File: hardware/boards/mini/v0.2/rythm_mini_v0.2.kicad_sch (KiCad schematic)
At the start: 99 parts, among them IC1 NAU88C22YG, IC3 IS42S16160J-6BLI, J2 Top, J3 Bottom, Q1 PMV37EN22, U1 W25Q128JVP, U2 LTV-217-G, U4 STM32H750XBHx, Y1 Crystal_GND24, Y3 Crystal

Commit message: mini: start BOM selection
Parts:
- C10, C11, C12, C13, C14, C33, C48, C5, C50, C51, C52, C54, C55, C56, C57, C58, C60, C61, C62, C63, C64, C67, C68, C7, C8, C9: JLC (none) -> C1525
- C16, C17, C18, C19, C28, C29, C36, C37, C38: JLC (none) -> C23733
- C20, C21, C22, C23, C24, C25, C26, C27, C31, C32, C6: JLC (none) -> C52923
- C30: JLC (none) -> C15195
- C34, C35, C69: JLC (none) -> C15525
- D1: footprint LED_SMD:LED_0402_1005Metric -> LED_SMD:LED_0603_1608Metric; JLC (none) -> C2286
- D2, D4: footprint LED_SMD:LED_0402_1005Metric -> LED_SMD:LED_0603_1608Metric; JLC (none) -> C89811
- IC3: JLC (none) -> C1351289
- J2, J3: JLC (none) -> C424647
- Q1: JLC (none) -> C478164
- R1, R2: JLC (none) -> C25900
- R10, R11, R12, R13, R14, R18, R5: JLC (none) -> C25744
- R3, R4: JLC (none) -> C25879
- R7: JLC (none) -> C25091
- U4: JLC (none) -> C405932
- Y3: value Crystal -> 32.768kHz

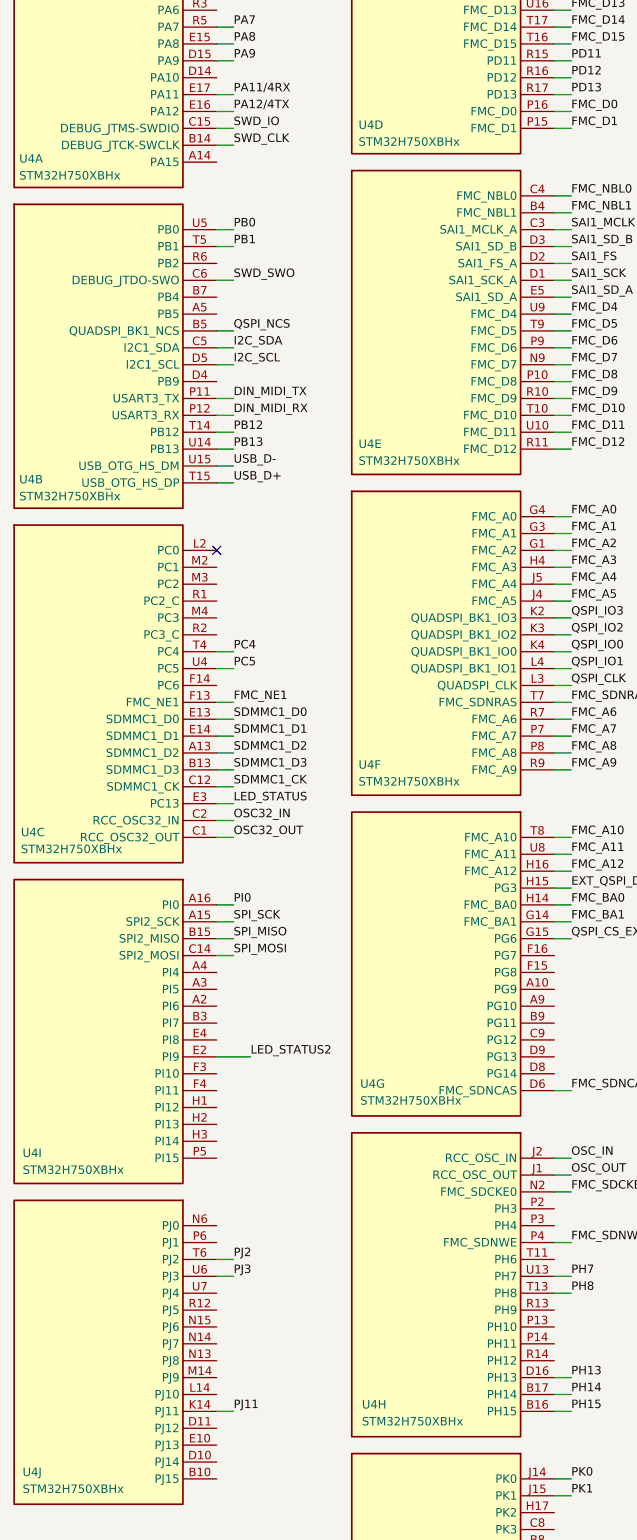
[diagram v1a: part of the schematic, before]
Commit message: mini: add Digikey part numbers to BOM
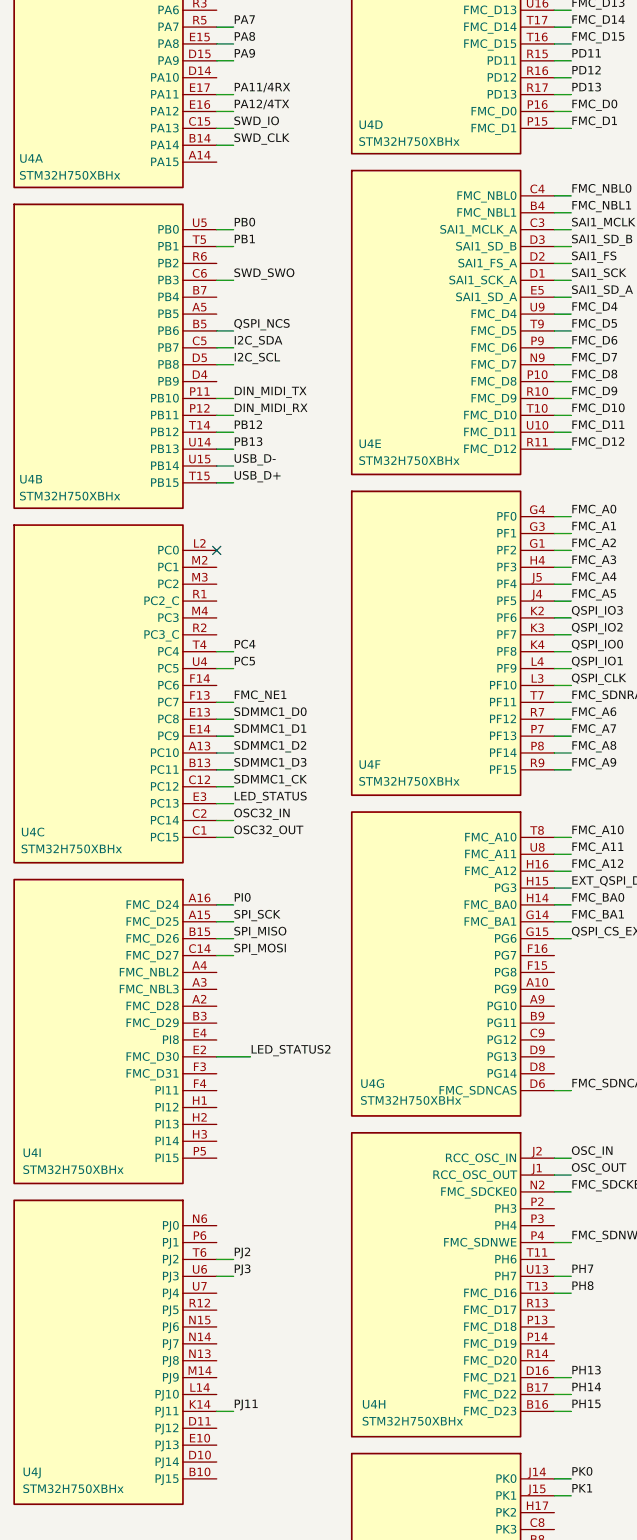
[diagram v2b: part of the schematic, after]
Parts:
- C10, C11, C12, C13, C14, C33, C48, C5, C50, C51, C52, C54, C55, C56, C57, C58, C60, C61, C62, C63, C64, C67, C68, C7, C8, C9: Digikey (none) -> 1276-CL05B104KP5VPNCCT-ND
- C16, C17, C18, C19, C28, C29, C36, C37, C38: Digikey (none) -> 1276-1482-1-ND
- C20, C21, C22, C23, C24, C25, C26, C27, C31, C32, C6: Digikey (none) -> 1276-1043-1-ND
- C30: Digikey (none) -> 399-C0402C103K4REC7411CT-ND
- C34, C35, C69: Digikey (none) -> 1276-1450-1-ND
- FB1: footprint Inductor_SMD:L_0805_2012Metric -> Inductor_SMD:L_0402_1005Metric; Digikey (none) -> 490-5203-1-ND
- FB2, FB3, FB4, FB5: footprint Inductor_SMD:L_0603_1608Metric -> Inductor_SMD:L_0402_1005Metric; Digikey (none) -> 490-5442-1-ND
- IC1: Digikey (none) -> NAU88C22YG-ND
- IC3: Digikey (none) -> 1450-1249-ND
- J2, J3: Digikey (none) -> H11628CT-ND
- Q1: Digikey (none) -> 1727-2306-1-ND
- R1, R2: Digikey (none) -> 311-4.7KJRCT-ND
- R10, R11, R12, R13, R14, R18, R5: Digikey (none) -> 311-10KJRCT-ND
- R3, R4: Digikey (none) -> RMCF0402FT2K20CT-ND
- R7: Digikey (none) -> A130044CT-ND
- U1: Digikey (none) -> 256-W25Q128JVPIQ-TUBE-ND
- U2: Digikey (none) -> 160-2218-1-ND
- U4: Digikey (none) -> 497-18111-ND
- Y3: Digikey (none) -> SER4103CT-ND
